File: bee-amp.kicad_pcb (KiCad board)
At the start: 2 copper layers, 29 x 53.3 mm, 33 parts, among them J1 Conn_01x02_Male, J10 Conn_01x02, J2 Conn_01x02_Male, J3 Conn_01x02_Male, J4 Conn_01x02_Male, J7 Conn_01x03, J8 Conn_01x02, J9 Conn_01x02, U1 OP07

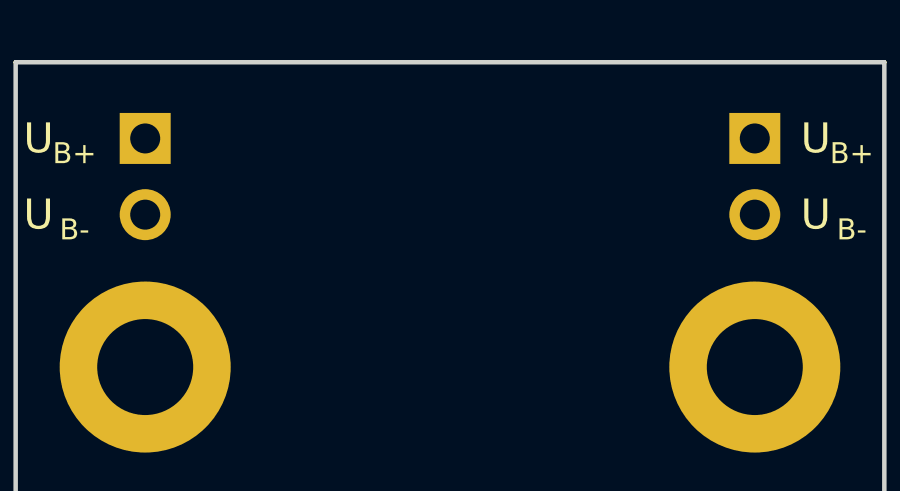
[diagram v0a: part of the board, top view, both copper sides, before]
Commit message: Add text and logos.
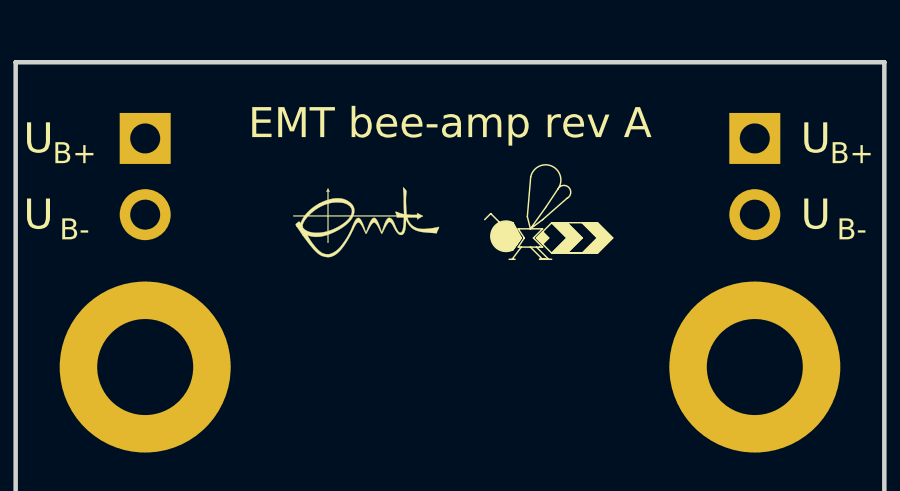
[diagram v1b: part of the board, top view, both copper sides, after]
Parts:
- added H13: Silkscreen_Label, Symbol-emt:EMT-Logo_5.1x2.5mm_Silkscreen, F.Cu at (86.1, 94.2)
- added H14: Silkscreen_Label, Symbol-emt:BEE-Logo_Silkscreen_small, F.Cu at (91.9, 94.7)
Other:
- board text added: "EMT bee-amp rev A"
